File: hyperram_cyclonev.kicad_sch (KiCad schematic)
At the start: 65 parts, among them IC1 AP63205WU, IC2 TXB0108PWR, IC3 S26KL128SDABHI020, IC4 W25Q32JVSSIQ_TR, IC5 S27KL0641DABHI020, J1 ASP-122952-01, J2 HDMI_A, J3 Conn_02x10_Odd_Even, J4 Conn_02x06_Odd_Even, J5 Conn_02x06_Top_Bottom, J6 Conn_02x06_Top_Bottom, J7 Conn_02x06_Top_Bottom, Q1 BSS138, Q2 BSS138

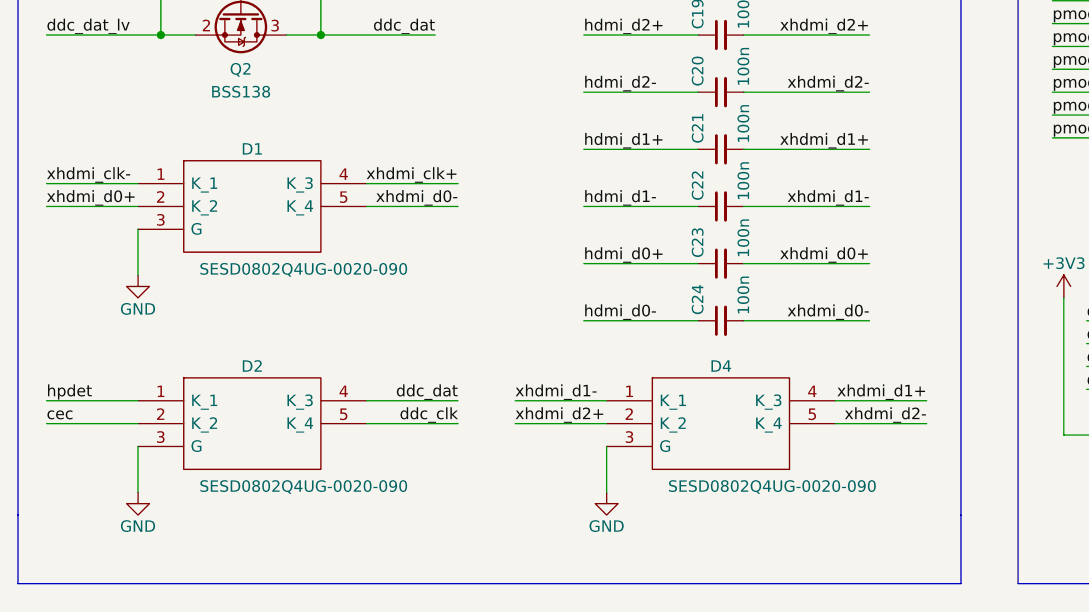
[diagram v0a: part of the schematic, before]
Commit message: Fixed signals connection to SESD Series TVS Diode Array
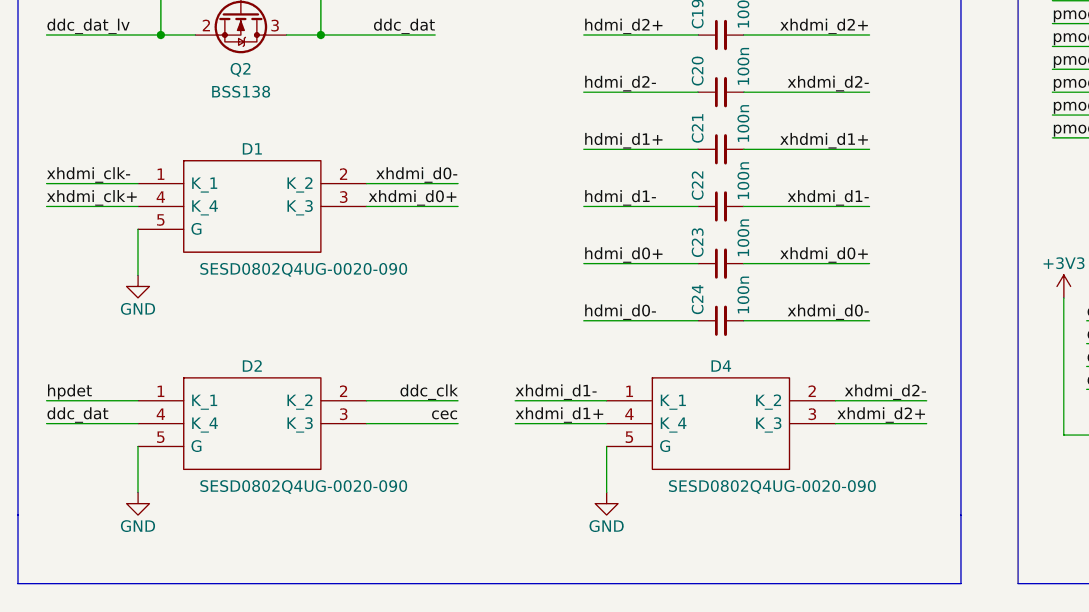
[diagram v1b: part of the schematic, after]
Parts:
- D1, D2, D4: footprint hyperram_cyclonev:SESD0802Q4UG0020090 -> SESD0802Q4UG0020090
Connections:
- net GND: now also D1.5 (G), D2.5 (G), D4.5 (G); no longer D1.3 (G), D2.3 (G), D4.3 (G)
- net cec: now also D2.3 (K_3); no longer D2.2 (K_2)
- net ddc_clk: now also D2.2 (K_2); no longer D2.5 (K_4)
- net xhdmi_d0+: now also D1.3 (K_3); no longer D1.2 (K_2)
- net xhdmi_d0-: now also D1.2 (K_2); no longer D1.5 (K_4)
- net xhdmi_d2+: now also D4.3 (K_3); no longer D4.2 (K_2)
- net xhdmi_d2-: now also D4.2 (K_2); no longer D4.5 (K_4)
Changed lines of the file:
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@@
 	)
 	(label "ddc_dat"
-		(at 64.77 152.4 180)
+		(at 19.05 154.94 0)
 		(fields_autoplaced yes)
 		(effects
@@
 				(size 1.27 1.27)
 			)
-			(justify right bottom)
+			(justify left bottom)
 		)
 	)
@@
 	)
 	(label "ddc_clk"
-		(at 64.77 154.94 180)
+		(at 64.77 152.4 180)
 		(fields_autoplaced yes)
 		(effects
@@
 	)
 	(label "xhdmi_d2+"
-		(at 71.12 154.94 0)
+		(at 116.84 154.94 180)
 		(fields_autoplaced yes)
 		(effects
@@
 				(size 1.27 1.27)
 			)
-			(justify left bottom)
+			(justify right bottom)
 		)
 	)
@@
 	)
 	(label "xhdmi_d0-"
-		(at 64.77 130.81 180)
+		(at 64.77 128.27 180)
 		(fields_autoplaced yes)
 		(effects
@@
 	)
 	(label "xhdmi_d1+"
-		(at 116.84 152.4 180)
+		(at 71.12 154.94 0)
 		(fields_autoplaced yes)
 		(effects
@@
 				(size 1.27 1.27)
 			)
-			(justify right bottom)
+			(justify left bottom)
 		)
 	)
@@
 	)
 	(label "cec"
-		(at 19.05 154.94 0)
+		(at 64.77 154.94 180)
 		(fields_autoplaced yes)
 		(effects
@@
 				(size 1.27 1.27)
 			)
-			(justify left bottom)
+			(justify right bottom)
 		)
 	)
@@
 	)
 	(label "xhdmi_d2-"
-		(at 116.84 154.94 180)
+		(at 116.84 152.4 180)
 		(fields_autoplaced yes)
 		(effects
@@
 	)
 	(label "xhdmi_clk+"
-		(at 64.77 128.27 180)
+		(at 19.05 130.81 0)
 		(fields_autoplaced yes)
 		(effects
@@
 				(size 1.27 1.27)
 			)
-			(justify right bottom)
+			(justify left bottom)
 		)
 	)
@@
 	)
 	(label "xhdmi_d0+"
-		(at 19.05 130.81 0)
+		(at 64.77 130.81 180)
 		(fields_autoplaced yes)
 		(effects
@@
 				(size 1.27 1.27)
 			)
-			(justify left bottom)
+			(justify right bottom)
 		)
 	)
@@
 	)
 	(symbol
+		(lib_name "SESD0802Q4UG-0020-090_2")
 		(lib_id "hyperram_cyclonev:SESD0802Q4UG-0020-090")
 		(at 29.21 152.4 0)
@@
 			)
 		)
-		(property "Footprint" "hyperram_cyclonev:SESD0802Q4UG0020090"
+		(property "Footprint" "SESD0802Q4UG0020090"
 			(at 50.8 149.86 0)
 			(effects
@@
 			)
 		)
-		(property "Footprint" "hyperram_cyclonev:SESD0802Q4UG0020090"
+		(property "Footprint" "SESD0802Q4UG0020090"
 			(at 102.87 149.86 0)
 			(effects
@@
 	)
 	(symbol
+		(lib_name "SESD0802Q4UG-0020-090_1")
 		(lib_id "hyperram_cyclonev:SESD0802Q4UG-0020-090")
 		(at 29.21 128.27 0)
@@
 			)
 		)
-		(property "Footprint" "hyperram_cyclonev:SESD0802Q4UG0020090"
+		(property "Footprint" "SESD0802Q4UG0020090"
 			(at 50.8 125.73 0)
 			(effects

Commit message: Changed SESD Series TVS Diode Array to different model. Rearranged schematic.
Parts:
- removed D1, D2, D4: SESD0802Q4UG-0020-090, SESD0802Q4UG0020090, symbol hyperram_cyclonev:SESD0802Q4UG-0020-090
- added D1, D2, D4: SESD1004Q4UG-0020-090, SESD1004Q4UG0020090, symbol hyperram_cyclonev:SESD1004Q4UG-0020-090
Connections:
- net GND: now also D1.3 (GND_1), D1.8 (GND_2), D2.3 (GND_1), D2.8 (GND_2), D4.3 (GND_1), D4.8 (GND_2)
- net cec: now also D2.5 (K_4), D2.6 (NC_1)
- net ddc_clk: now also D2.4 (K_3), D2.7 (NC_2)
- net ddc_dat: now also D2.2 (K_2), D2.9 (NC_3)
- net hpdet: now also D2.1 (K_1), D2.10 (NC_4)
- net xhdmi_clk+: now also D1.2 (K_2), D1.9 (NC_3)
- net xhdmi_clk-: now also D1.1 (K_1), D1.10 (NC_4)
- net xhdmi_d0+: now also D1.5 (K_4), D1.6 (NC_1)
- net xhdmi_d0-: now also D1.4 (K_3), D1.7 (NC_2)
- net xhdmi_d1+: now also D4.2 (K_2), D4.9 (NC_3)
- net xhdmi_d1-: now also D4.1 (K_1), D4.10 (NC_4)
- net xhdmi_d2+: now also D4.5 (K_4), D4.6 (NC_1)
- net xhdmi_d2-: now also D4.4 (K_3), D4.7 (NC_2)
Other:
- moved on the sheet: C1, C10, C11, C12, C13, C14, C15, C17, C18, C19, C2, C20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

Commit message: Updated footprints for changed SESD Series TVS Diode Arrays
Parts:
- D1, D2, D4: footprint SESD1004Q4UG0020090 -> hyperram_cyclonev:SESD1004Q4UG0020090
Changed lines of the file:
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@@
 			)
 		)
-		(property "Footprint" "SESD1004Q4UG0020090"
+		(property "Footprint" "hyperram_cyclonev:SESD1004Q4UG0020090"
 			(at 119.38 249.86 0)
 			(effects
@@
 			)
 		)
-		(property "Footprint" "SESD1004Q4UG0020090"
+		(property "Footprint" "hyperram_cyclonev:SESD1004Q4UG0020090"
 			(at 58.42 224.46 0)
 			(effects
@@
 			)
 		)
-		(property "Footprint" "SESD1004Q4UG0020090"
+		(property "Footprint" "hyperram_cyclonev:SESD1004Q4UG0020090"
 			(at 58.42 249.86 0)
 			(effects

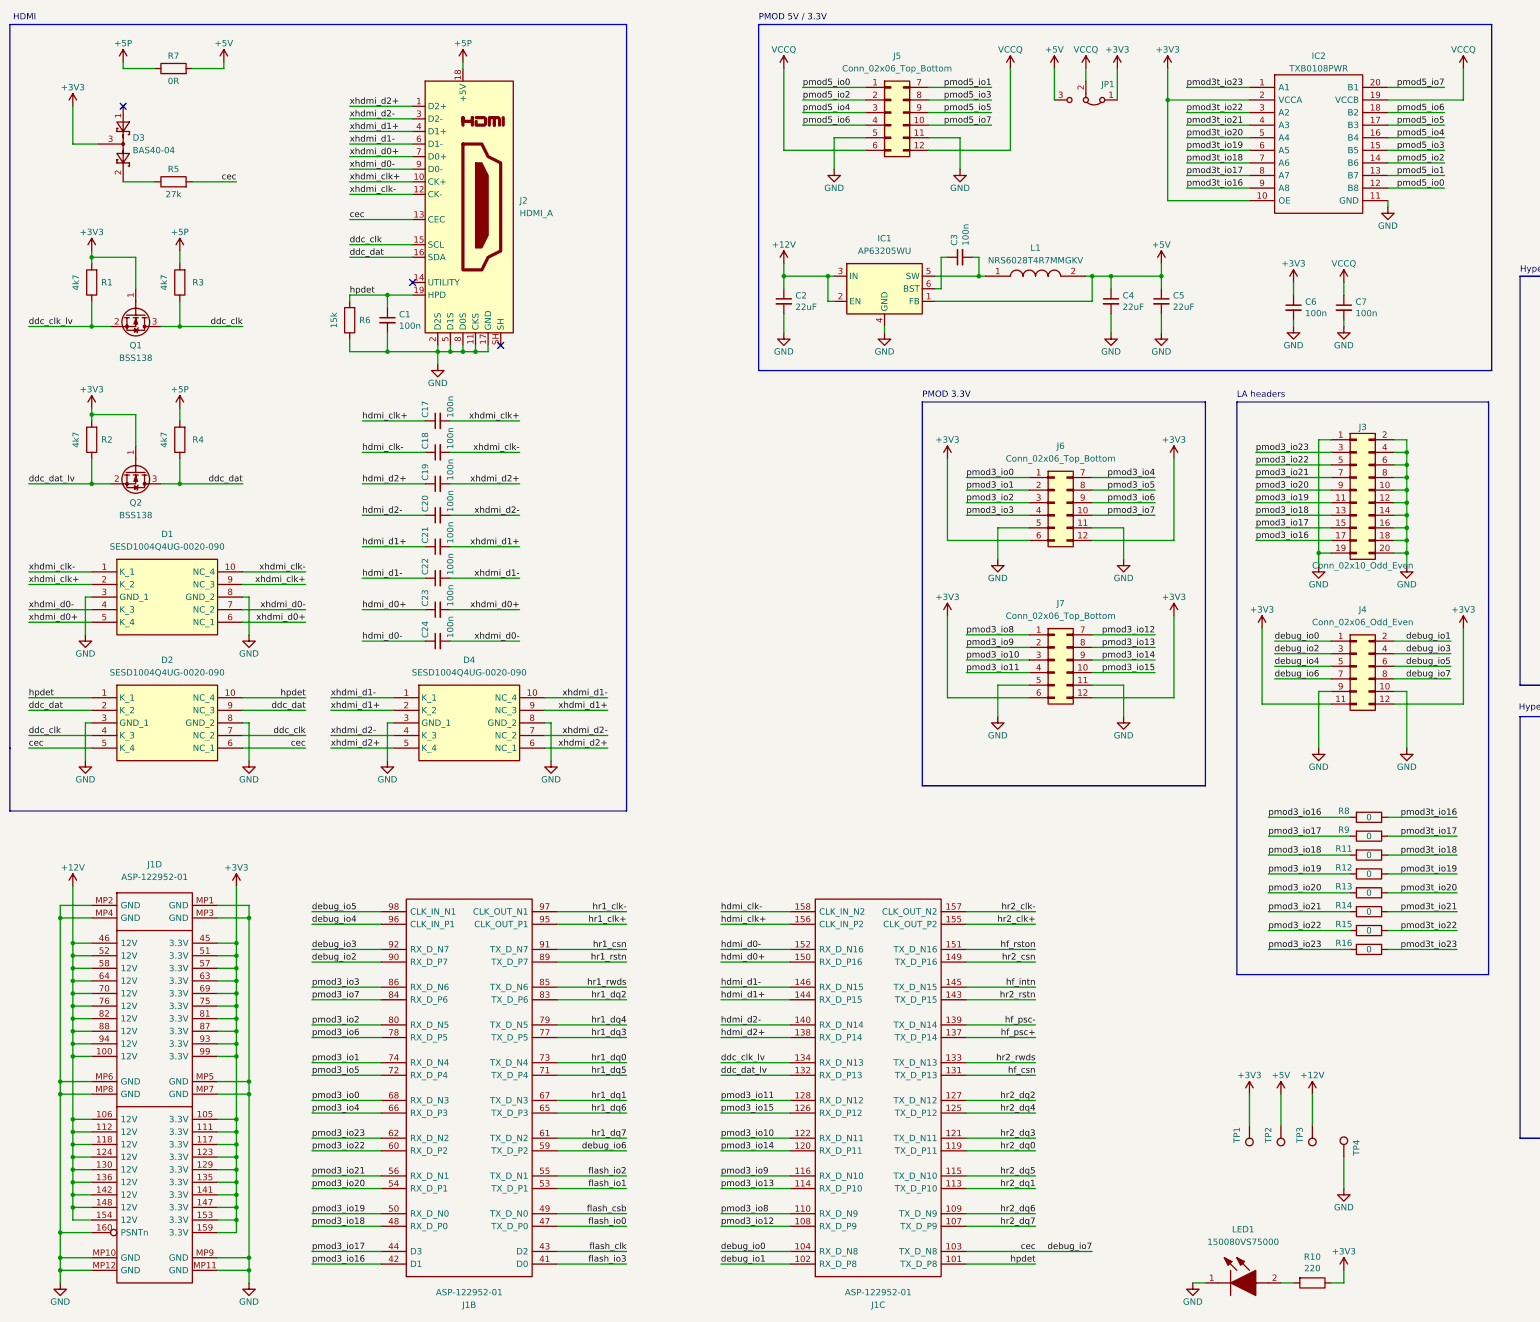
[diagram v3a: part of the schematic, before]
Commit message: Connected directly +5P with +5V power
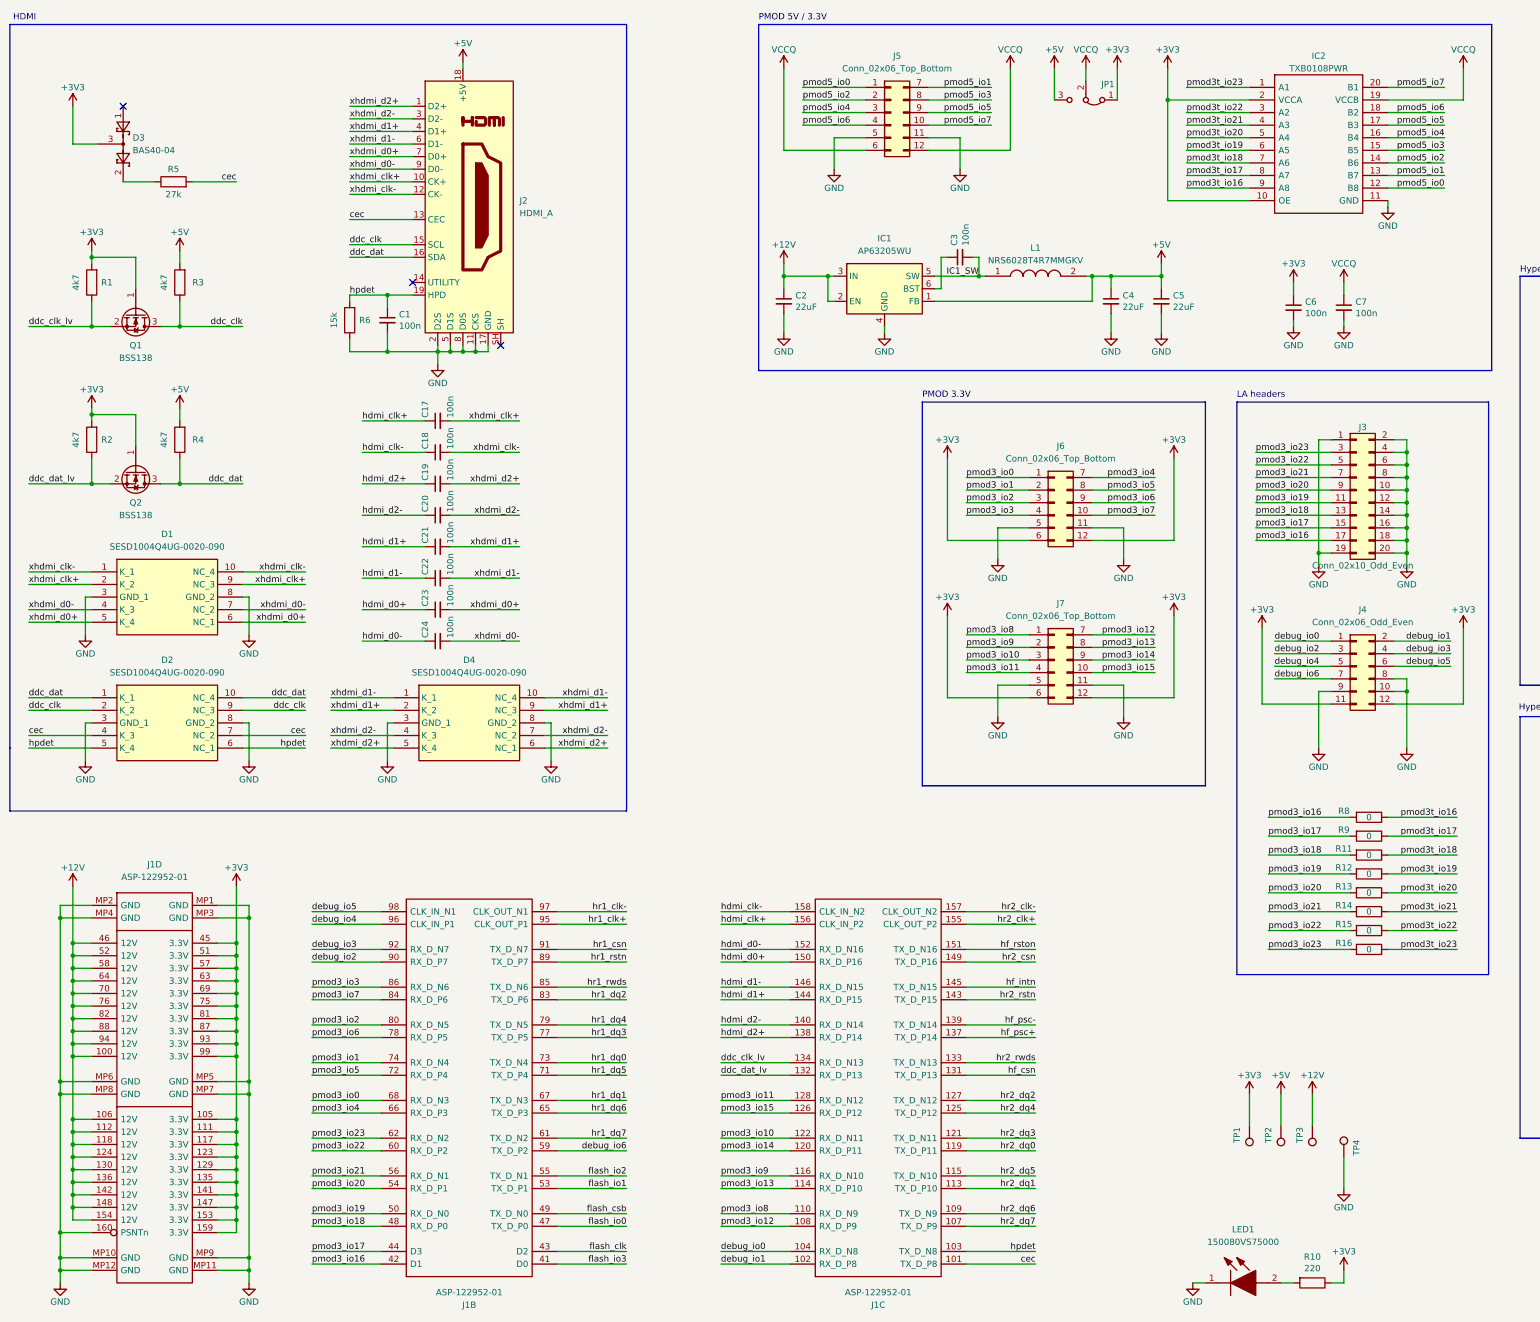
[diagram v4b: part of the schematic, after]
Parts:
- removed R7: 0R, Resistor_SMD:R_0603_1608Metric_Pad0.98x0.95mm_HandSolder, symbol Device:R
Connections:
- net +5P is gone; now on net +5V: J2.18 (+5V), R3.2, R4.2
- net GND: now also J4.8 (Pin_8)
- net cec: now also D2.4 (K_3), D2.7 (NC_2), J1.101 (TX_D_P8); no longer D2.5 (K_4), D2.6 (NC_1), J1.103 (TX_D_N8), J4.8 (Pin_8)
- net ddc_clk: now also D2.2 (K_2), D2.9 (NC_3); no longer D2.4 (K_3), D2.7 (NC_2)
- net ddc_dat: now also D2.1 (K_1), D2.10 (NC_4); no longer D2.2 (K_2), D2.9 (NC_3)
- net hpdet: now also D2.5 (K_4), D2.6 (NC_1), J1.103 (TX_D_N8); no longer D2.1 (K_1), D2.10 (NC_4), J1.101 (TX_D_P8)
- net IC1_SW: now reaches C3.2, IC1.5 (SW), L1.1
